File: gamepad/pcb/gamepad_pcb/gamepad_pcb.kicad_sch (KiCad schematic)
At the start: 9 parts, among them J1 RP CON R, J2 RP CON L, J3 JOYSTICK, SW1 BTN MINUS, SW2 BTN PLUS, SW3 BTN NORTH, SW4 BTN EAST, SW5 BTN SOUTH, SW6 BTN WEST

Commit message: feat: working on pcb
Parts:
- removed J1: RP CON R, Connector_PinSocket_2.54mm:PinSocket_1x20_P2.54mm_Vertical, symbol Connector:Conn_01x20_Pin
- removed J2: RP CON L, Connector_PinSocket_2.54mm:PinSocket_1x20_P2.54mm_Vertical, symbol Connector:Conn_01x20_Pin
- added U1: Pico, RPi_Pico:RPi_Pico_SMD_TH, symbol MCU_RaspberryPi_and_Boards:Pico
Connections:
- net GND: now reaches SW5.1
- net GND: now also J3.5 (Pin_5), SW1.1, SW2.1, SW3.1, SW4.1, SW6.1, U1.8 (GND)
- net at J3.1 (Pin_1): now also U1.20 (GPIO15)
- net at J3.3 (Pin_3): now also U1.31 (GPIO26_ADC0)
- net +3V3: now reaches J3.4 (Pin_4)
- net +3V3: now also U1.36 (3V3)
- net at J3.2 (Pin_2): now also U1.32 (GPIO27_ADC1)
- new net: SW5.2, U1.15 (GPIO11)
- new net: SW4.2, U1.14 (GPIO10)
- new net: SW3.2, U1.16 (GPIO12)
- new net: SW6.2, U1.17 (GPIO13)
- new net: SW1.2, U1.18 (GND)
- new net: SW2.2, U1.19 (GPIO14)
- no-connect marks 29 -> 32
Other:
- note removed: "GP0 GP1 GND GP2 GP3 GP4 GP5 GND GP6 GP7 GP9 GND GP10 GP11 GP12 GP13 GND GP14 GP15"
- note removed: "VBUS VSYS GND 3v3_EN 3v3(OUT) ADC_VREF GP28 GND GP17 GP26 RUN GP22 GND GP21 GP20 GP19 GP18 GND GP17 GP16"
- company: (none) -> ONYX Development
- title: (none) -> Andrew Arcade Controller
- moved on the sheet: J3, SW1, SW2, SW3, SW4, SW5, SW6

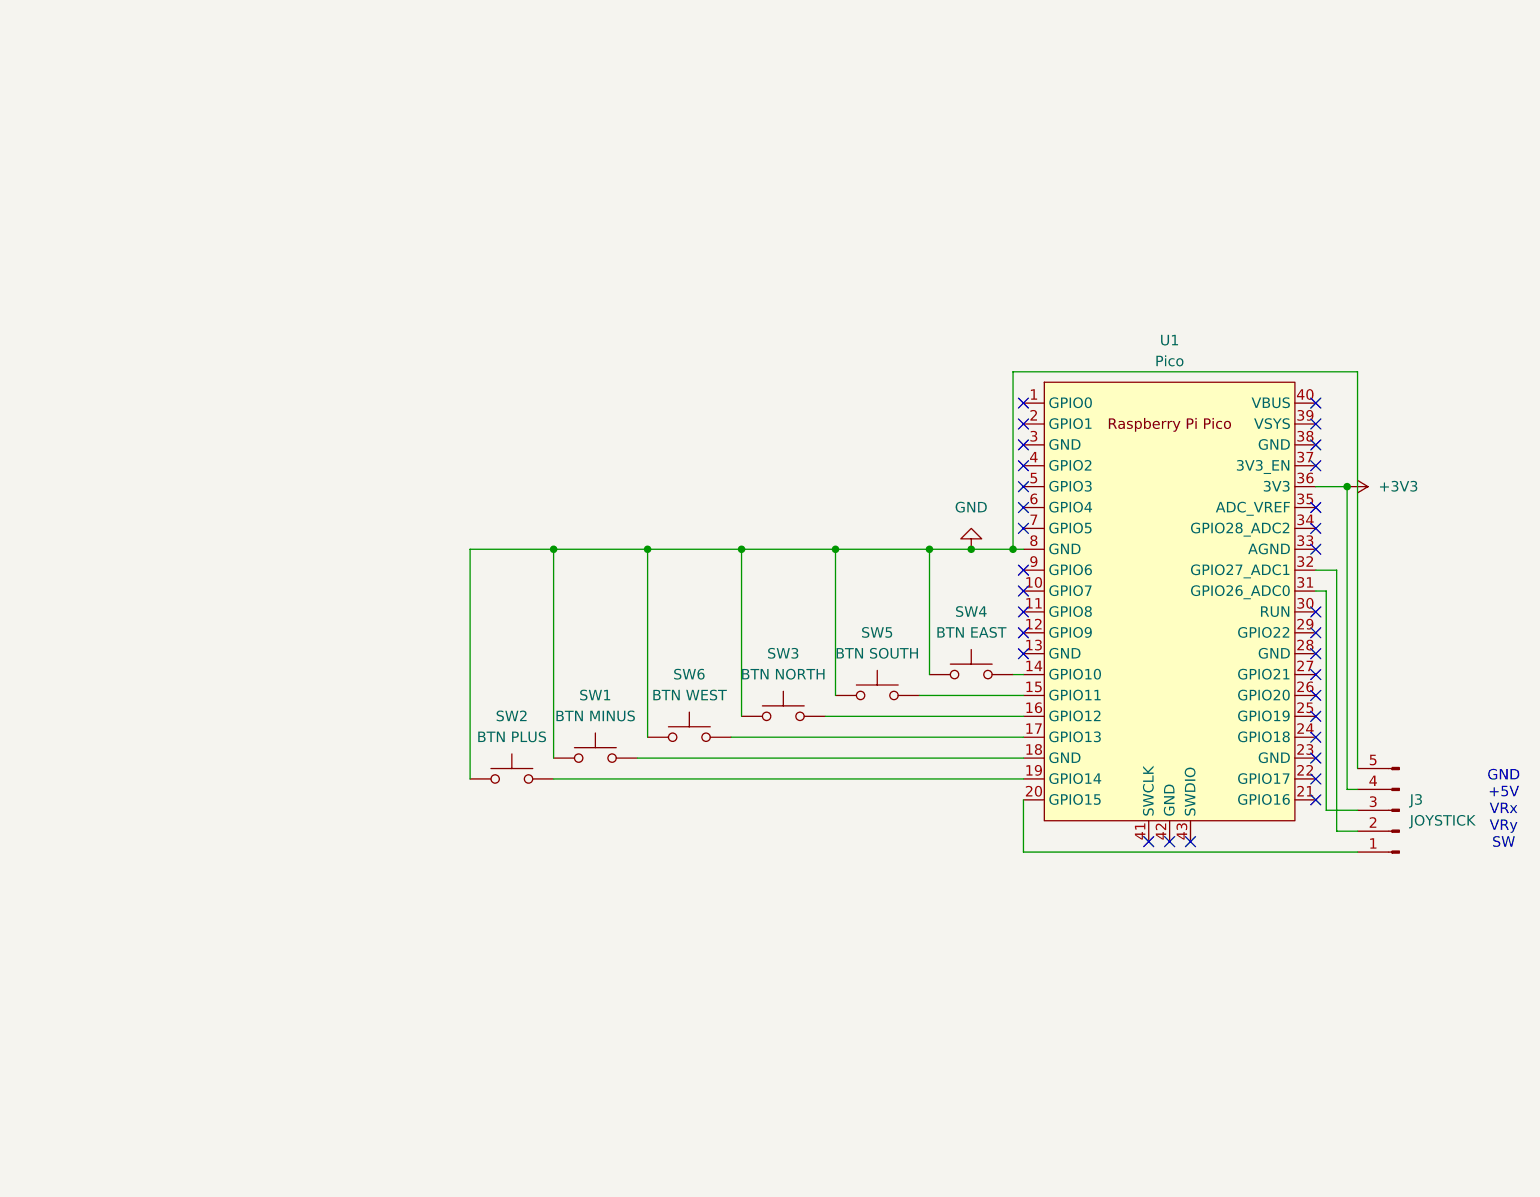
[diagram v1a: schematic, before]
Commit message: fix: controller schematic
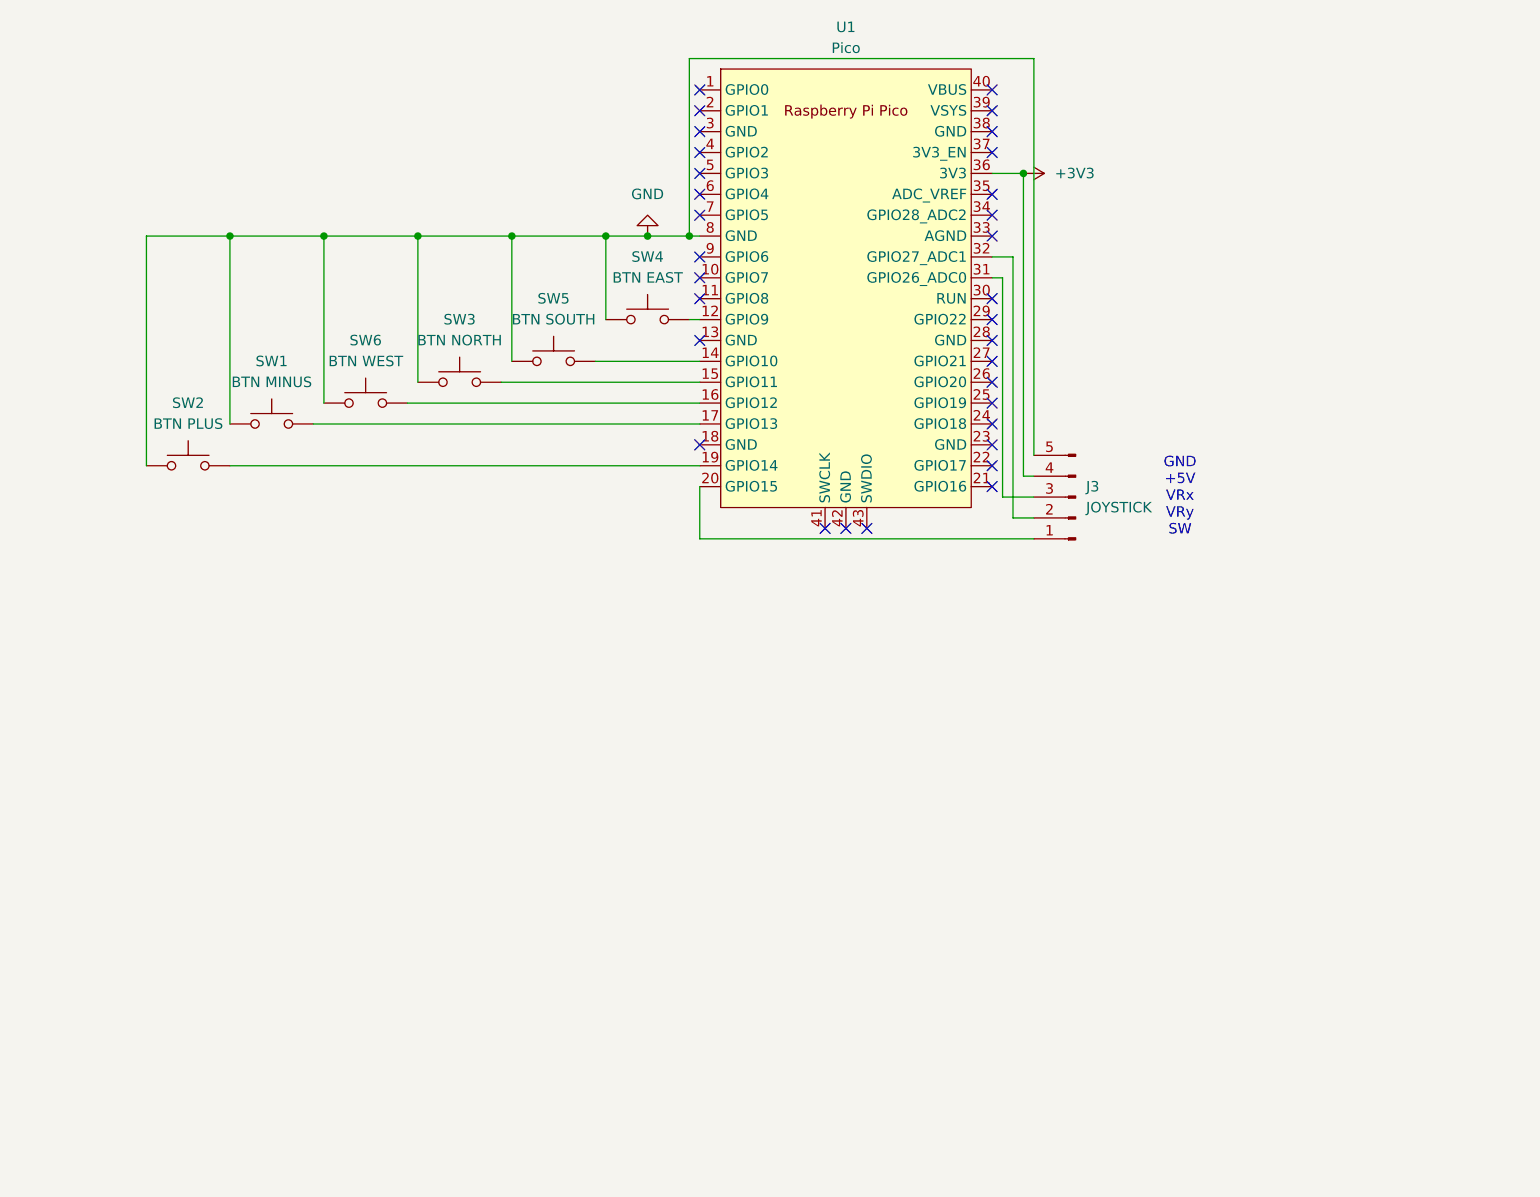
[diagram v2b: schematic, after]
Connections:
- net at SW5.2: now also U1.14 (GPIO10); no longer U1.15 (GPIO11)
- net at SW4.2: now also U1.12 (GPIO9); no longer U1.14 (GPIO10)
- net at SW3.2: now also U1.15 (GPIO11); no longer U1.16 (GPIO12)
- net at SW6.2: now also U1.16 (GPIO12); no longer U1.17 (GPIO13)
- net at SW1.2: now also U1.17 (GPIO13); no longer U1.18 (GND)
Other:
- moved on the sheet: J3, SW1, SW2, SW3, SW4, SW5, SW6, U1

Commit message: upt: schematic
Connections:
- net at U1.31 (GPIO26_ADC0): now also J3.2 (Pin_2); no longer J3.3 (Pin_3)
- net at U1.32 (GPIO27_ADC1): now also J3.3 (Pin_3); no longer J3.2 (Pin_2)
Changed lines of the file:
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@@
+	(wire
+		(pts
+			(xy 142.24 58.42) (xy 139.7 58.42)
+		)
+		(stroke
+			(width 0)
+			(type default)
+		)
+	)
 	(wire
 		(pts
@@
 	(wire
 		(pts
+			(xy 140.97 90.17) (xy 144.78 90.17)
+		)
+		(stroke
+			(width 0)
+			(type default)
+		)
+	)
+	(wire
+		(pts
 			(xy 46.99 55.88) (xy 46.99 78.74)
 		)
@@
 	(wire
 		(pts
-			(xy 144.78 90.17) (xy 142.24 90.17)
+			(xy 140.97 60.96) (xy 140.97 90.17)
+		)
+		(stroke
+			(width 0)
+			(type default)
+		)
+	)
+	(wire
+		(pts
+			(xy 144.78 87.63) (xy 142.24 87.63)
 		)
 		(stroke
@@
 	(wire
 		(pts
-			(xy 142.24 58.42) (xy 142.24 90.17)
-		)
-		(stroke
-			(width 0)
-			(type default)
-		)
-	)
-	(wire
-		(pts
 			(xy 139.7 48.26) (xy 143.51 48.26)
 		)
@@
 	(wire
 		(pts
-			(xy 140.97 60.96) (xy 140.97 87.63)
-		)
-		(stroke
-			(width 0)
-			(type default)
-		)
-	)
-	(wire
-		(pts
 			(xy 97.79 55.88) (xy 92.71 55.88)
 		)
@@
 	(wire
 		(pts
+			(xy 142.24 87.63) (xy 142.24 58.42)
+		)
+		(stroke
+			(width 0)
+			(type default)
+		)
+	)
+	(wire
+		(pts
 			(xy 57.15 78.74) (xy 104.14 78.74)
 		)
@@
 	(wire
 		(pts
-			(xy 144.78 87.63) (xy 140.97 87.63)
-		)
-		(stroke
-			(width 0)
-			(type default)
-		)
-	)
-	(wire
-		(pts
 			(xy 102.87 34.29) (xy 102.87 55.88)
 		)
@@
 		)
 		(stroke
-			(width 0)
-			(type default)
-		)
-	)
-	(wire
-		(pts
-			(xy 142.24 58.42) (xy 139.7 58.42)
-		)
-		(stroke
